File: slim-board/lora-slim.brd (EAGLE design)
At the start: 16.6 x 72.9 mm, 27 parts, among them IC1 STM32F030F4, IC2 ADP1607, J1 SWD_PTH_SHROUD, X1 SMA-142-0701-801/806, X2 UBLOX_MAX, X3 RFM98

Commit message: couple drc fixes
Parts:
- moved IC2 0.76 mm to (8.89, 31.8)
- moved R3 0.65 mm to (7.49, 29.5), turned to 180 degrees
- moved C6 0.25 mm to (9.02, 36.2)
- moved C3 0.25 mm to (8.76, 34.0)
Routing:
- net +3V3: track 117.5 -> 111.9 mm
- net RST: track 26.5 -> 27.4 mm
- net N$3: track 5.38 -> 6.14 mm
- net UART_RX: track 25.5 -> 24.9 mm
- net VBAT: track 61.6 -> 62.2 mm
- net GND: track 69.1 -> 69.5 mm, vias 130 -> 129

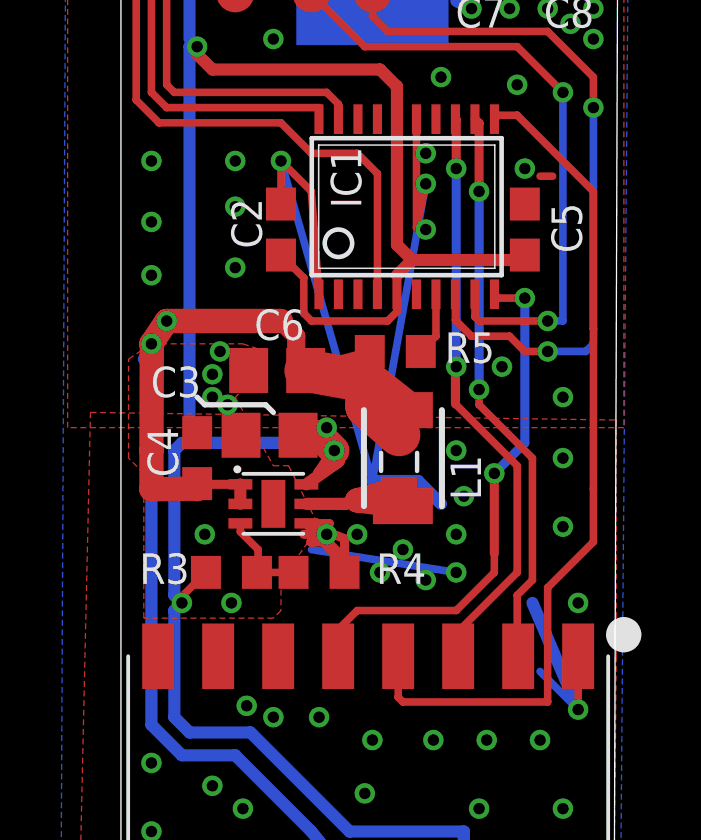
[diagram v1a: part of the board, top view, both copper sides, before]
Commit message: connecting clkout
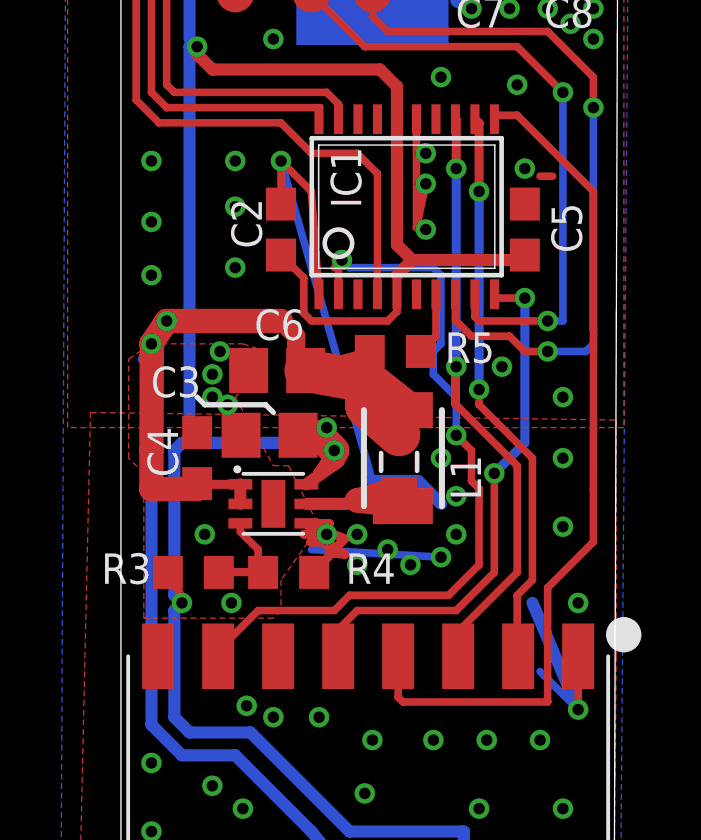
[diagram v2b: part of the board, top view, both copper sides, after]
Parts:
- moved R3 1.27 mm to (6.22, 29.5)
- moved R4 1.02 mm to (9.40, 29.5)
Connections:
- removed net GPIO2: IC1.2
- new net CLK: IC1.2, X3.7
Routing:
- net CLK: track 0.00 -> 25.5 mm, vias 0 -> 2
- net GND: track 69.5 -> 59.3 mm
- net N$6: track 3.12 -> 4.63 mm
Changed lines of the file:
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@@
 <layer number="21" name="tPlace" color="7" fill="1" visible="no" active="yes"/>
 <layer number="22" name="bPlace" color="7" fill="1" visible="yes" active="yes"/>
-<layer number="23" name="tOrigins" color="15" fill="1" visible="no" active="yes"/>
-<layer number="24" name="bOrigins" color="15" fill="1" visible="yes" active="yes"/>
+<layer number="23" name="tOrigins" color="15" fill="1" visible="yes" active="yes"/>
+<layer number="24" name="bOrigins" color="15" fill="1" visible="no" active="yes"/>
 <layer number="25" name="tNames" color="7" fill="1" visible="no" active="yes"/>
 <layer number="26" name="bNames" color="7" fill="1" visible="yes" active="yes"/>
 <layer number="27" name="tValues" color="7" fill="1" visible="no" active="yes"/>
 <layer number="28" name="bValues" color="7" fill="1" visible="yes" active="yes"/>
-<layer number="29" name="tStop" color="7" fill="3" visible="no" active="yes"/>
-<layer number="30" name="bStop" color="7" fill="6" visible="yes" active="yes"/>
+<layer number="29" name="tStop" color="7" fill="3" visible="yes" active="yes"/>
+<layer number="30" name="bStop" color="7" fill="6" visible="no" active="yes"/>
 <layer number="31" name="tCream" color="7" fill="4" visible="no" active="yes"/>
 <layer number="32" name="bCream" color="7" fill="5" visible="no" active="yes"/>
@@
 <attribute name="NAME" x="15.8115" y="31.877" size="1.016" layer="25" font="vector" ratio="13" rot="R90"/>
 </element>
-<element name="R3" library="rcl" package="R0603" value="360k" x="7.493" y="29.464" smashed="yes" rot="R180">
-<attribute name="NAME" x="6.096" y="30.099" size="1.016" layer="25" font="vector" ratio="13" rot="R180"/>
-</element>
-<element name="R4" library="rcl" package="R0603" value="220k" x="10.414" y="29.464" smashed="yes" rot="R180">
-<attribute name="NAME" x="12.319" y="29.083" size="1.016" layer="25" font="vector" ratio="13"/>
+<element name="R3" library="rcl" package="R0603" value="360k" x="6.223" y="29.464" smashed="yes" rot="R180">
+<attribute name="NAME" x="4.826" y="30.099" size="1.016" layer="25" font="vector" ratio="13" rot="R180"/>
+</element>
+<element name="R4" library="rcl" package="R0603" value="220k" x="9.398" y="29.464" smashed="yes" rot="R180">
+<attribute name="NAME" x="11.303" y="29.083" size="1.016" layer="25" font="vector" ratio="13"/>
 </element>
 <element name="C3" library="rcl" package="C0805" value="10u" x="8.763" y="34.036" smashed="yes" rot="R180">
@@
 <via x="9.144" y="43.18" extent="1-16" drill="0.381" shape="octagon"/>
 <wire x1="9.144" y1="43.18" x2="12.192" y2="32.512" width="0.254" layer="16"/>
-<wire x1="12.192" y1="32.512" x2="13.97" y2="42.418" width="0.254" layer="16"/>
 <via x="13.97" y="42.418" extent="1-16" drill="0.381" shape="octagon"/>
 <wire x1="18.2" y1="42.672" x2="17.78" y2="42.672" width="0.254" layer="1"/>
-<via x="13.97" y="29.21" extent="1-16" drill="0.381" shape="octagon"/>
+<via x="13.462" y="29.718" extent="1-16" drill="0.381" shape="octagon"/>
 <via x="6.858" y="36.068" extent="1-16" drill="0.381" shape="octagon"/>
 <via x="10.668" y="30.734" extent="1-16" drill="0.381" shape="octagon"/>
-<via x="14.986" y="29.464" extent="1-16" drill="0.381" shape="octagon"/>
+<via x="14.478" y="29.972" extent="1-16" drill="0.381" shape="octagon"/>
 <wire x1="9.056" y1="41.656" x2="9.144" y2="41.744" width="0.4064" layer="1"/>
 <wire x1="12.7" y1="7.024" x2="14.136" y2="7.278" width="0.4064" layer="1"/>
@@
 <wire x1="14.478" y1="5.588" x2="16.51" y2="6.858" width="0.254" layer="16"/>
 <wire x1="17.272" y1="6.858" x2="16.51" y2="6.858" width="0.254" layer="16"/>
-<wire x1="14.986" y1="29.464" x2="10.16" y2="30.226" width="0.254" layer="16"/>
+<wire x1="14.478" y1="29.972" x2="10.16" y2="30.226" width="0.254" layer="16"/>
 <polygon width="0.254" layer="16" isolate="0.3048">
 <vertex x="2.032" y="64.008"/>
@@
 <via x="6.35" y="61.976" extent="1-16" drill="0.381" shape="octagon"/>
 <via x="4.826" y="60.198" extent="1-16" drill="0.381" shape="octagon"/>
-<via x="15.24" y="32.004" extent="1-16" drill="0.381" shape="octagon"/>
-<wire x1="11.264" y1="29.464" x2="11.264" y2="30.588" width="0.3048" layer="1"/>
+<via x="14.986" y="32.004" extent="1-16" drill="0.381" shape="octagon"/>
+<wire x1="10.248" y1="29.464" x2="11.264" y2="30.588" width="0.3048" layer="1"/>
 <wire x1="11.264" y1="30.588" x2="9.99" y2="31.1" width="0.3048" layer="1"/>
 <wire x1="9.99" y1="31.1" x2="10.752" y2="30.260075" width="0.3048" layer="1"/>
@@
 <via x="7.493" y="28.448" extent="1-16" drill="0.381" shape="octagon"/>
 <via x="6.604" y="30.734" extent="1-16" drill="0.381" shape="octagon"/>
-<via x="12.446" y="29.464" extent="1-16" drill="0.381" shape="octagon"/>
-<via x="13.208" y="30.226" extent="1-16" drill="0.381" shape="octagon"/>
+<via x="11.684" y="29.718" extent="1-16" drill="0.381" shape="octagon"/>
+<via x="12.7" y="30.226" extent="1-16" drill="0.381" shape="octagon"/>
 <via x="14.986" y="30.734" extent="1-16" drill="0.381" shape="octagon"/>
-<via x="14.986" y="33.528" extent="1-16" drill="0.381" shape="octagon"/>
+<via x="14.478" y="33.274" extent="1-16" drill="0.381" shape="octagon"/>
 <via x="18.542" y="30.988" extent="1-16" drill="0.381" shape="octagon"/>
 <via x="18.542" y="35.306" extent="1-16" drill="0.381" shape="octagon"/>
@@
 <wire x1="7.79" y1="30.818" x2="8.382" y2="30.226" width="0.254" layer="1"/>
 <wire x1="8.382" y1="30.226" x2="8.382" y2="29.503" width="0.254" layer="1"/>
-<wire x1="8.382" y1="29.503" x2="8.343" y2="29.464" width="0.254" layer="1"/>
-<wire x1="9.564" y1="29.464" x2="8.343" y2="29.464" width="0.254" layer="1"/>
+<wire x1="8.382" y1="29.503" x2="7.073" y2="29.464" width="0.254" layer="1"/>
+<wire x1="8.548" y1="29.464" x2="7.073" y2="29.464" width="0.254" layer="1"/>
 </signal>
 <signal name="+3V3">
@@
 <wire x1="5.588" y1="28.194" x2="5.842" y2="28.448" width="0.4064" layer="16"/>
 <wire x1="5.842" y1="28.448" x2="5.842" y2="28.663" width="0.254" layer="1"/>
-<wire x1="5.842" y1="28.663" x2="6.643" y2="29.464" width="0.254" layer="1"/>
+<wire x1="5.842" y1="28.663" x2="5.373" y2="29.464" width="0.254" layer="1"/>
 <wire x1="5.588" y1="33.528" x2="5.588" y2="28.702" width="0.4064" layer="16"/>
 <wire x1="5.588" y1="28.702" x2="5.842" y2="28.448" width="0.4064" layer="16"/>
@@
 <contactref element="IC1" pad="6"/>
 </signal>
-<signal name="GPIO2">
-<contactref element="IC1" pad="2"/>
-</signal>
 <signal name="NSS">
 <contactref element="IC1" pad="10"/>
@@
 <wire x1="11.684" y1="28.194" x2="14.986" y2="28.194" width="0.254" layer="1"/>
 <wire x1="14.986" y1="28.194" x2="16.256" y2="29.464" width="0.254" layer="1"/>
-<wire x1="16.256" y1="29.464" x2="16.256" y2="30.0982" width="0.254" layer="1"/>
+<wire x1="16.256" y1="29.464" x2="16.256" y2="32.6382" width="0.254" layer="1"/>
 <via x="17.272" y="38.608" extent="1-16" drill="0.381" shape="octagon"/>
 <wire x1="17.272" y1="38.608" x2="16.3902" y2="38.608" width="0.254" layer="1"/>
@@
 <wire x1="16.256" y1="32.766" x2="17.272" y2="33.782" width="0.3048" layer="16"/>
 <wire x1="17.272" y1="33.782" x2="17.272" y2="38.608" width="0.3048" layer="16"/>
-<wire x1="16.256" y1="30.0982" x2="16.256" y2="32.766" width="0.3048" layer="1"/>
+<wire x1="16.256" y1="32.6382" x2="16.256" y2="32.766" width="0.3048" layer="1"/>
 </signal>
 <signal name="N$9">
@@
 <wire x1="17.018" y1="63.246" x2="16.598" y2="63.246" width="0.254" layer="1"/>
 </signal>
+<signal name="CLK">
+<contactref element="X3" pad="7"/>
+<contactref element="IC1" pad="2"/>
+<wire x1="7.05" y1="26.67" x2="7.05" y2="26.862" width="0.254" layer="1"/>
+<wire x1="7.05" y1="26.862" x2="8.382" y2="28.194" width="0.254" layer="1"/>
+<wire x1="8.382" y1="28.194" x2="10.922" y2="28.194" width="0.254" layer="1"/>
+<wire x1="10.922" y1="28.194" x2="11.43" y2="28.702" width="0.254" layer="1"/>
+<wire x1="11.43" y1="28.702" x2="14.732" y2="28.702" width="0.254" layer="1"/>
+<wire x1="14.732" y1="28.702" x2="15.748" y2="29.718" width="0.254" layer="1"/>
+<wire x1="15.748" y1="29.718" x2="15.748" y2="32.258" width="0.254" layer="1"/>
+<wire x1="15.748" y1="32.258" x2="15.494" y2="32.512" width="0.254" layer="1"/>
+<wire x1="15.494" y1="32.512" x2="15.494" y2="33.528" width="0.254" layer="1"/>
+<wire x1="15.494" y1="33.528" x2="14.986" y2="34.036" width="0.254" layer="1"/>
+<via x="14.986" y="34.036" extent="1-16" drill="0.381" shape="octagon"/>
+<wire x1="14.986" y1="34.036" x2="14.986" y2="35.306" width="0.254" layer="16"/>
+<wire x1="14.986" y1="35.306" x2="14.224" y2="36.068" width="0.254" layer="16"/>
+<wire x1="14.224" y1="36.068" x2="14.224" y2="36.83" width="0.254" layer="16"/>
+<wire x1="14.224" y1="36.83" x2="14.478" y2="37.084" width="0.254" layer="16"/>
+<wire x1="14.478" y1="37.084" x2="14.478" y2="39.37" width="0.254" layer="16"/>
+<wire x1="14.478" y1="39.37" x2="14.224" y2="39.624" width="0.254" layer="16"/>
+<wire x1="14.224" y1="39.624" x2="11.43" y2="39.624" width="0.254" layer="16"/>
+<wire x1="11.43" y1="39.624" x2="11.176" y2="39.878" width="0.254" layer="16"/>
+<via x="11.176" y="39.878" extent="1-16" drill="0.381" shape="octagon"/>
+<wire x1="11.176" y1="39.878" x2="10.922" y2="39.624" width="0.254" layer="1"/>
+<wire x1="11.06" y1="38.7382" x2="11.06" y2="39.762" width="0.254" layer="1"/>
+<wire x1="11.06" y1="39.762" x2="11.176" y2="39.878" width="0.254" layer="1"/>
+</signal>
 </signals>

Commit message: adding copyright notice
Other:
- board text added: "©"
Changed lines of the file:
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@@
 <wire x1="6.604" y1="35.052" x2="8.636" y2="35.052" width="0.1778" layer="21"/>
 <wire x1="8.636" y1="35.052" x2="8.89" y2="34.798" width="0.1778" layer="21"/>
+<text x="18.288" y="27.178" size="1.27" layer="22" rot="MR0">©</text>
 </plain>
 <attributes>
